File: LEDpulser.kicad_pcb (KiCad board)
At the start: 2 copper layers, 38.2 x 98.2 mm, 72 parts, among them J1 RJHSE5380, J2 EPS.00.250.NTN, J3 EPS.00.250.NTN, J4 Conn_01x04_Female, J5 LED, Q1 AO3401A, Q2 AO3400A, Q3 AO3400A, SW1 BST11T2AVR, U1 SN74AHCT123A, U10 LT3082, U11 SN74HCS72, U2 SN74AHCT123A, U3 SN74AHCT123A, U4 74HC10, U4 SN74AHCT123A, U5 LT1121-5, U6 PM8834, U7 NE555, U8 PM8834, U9 PM8834

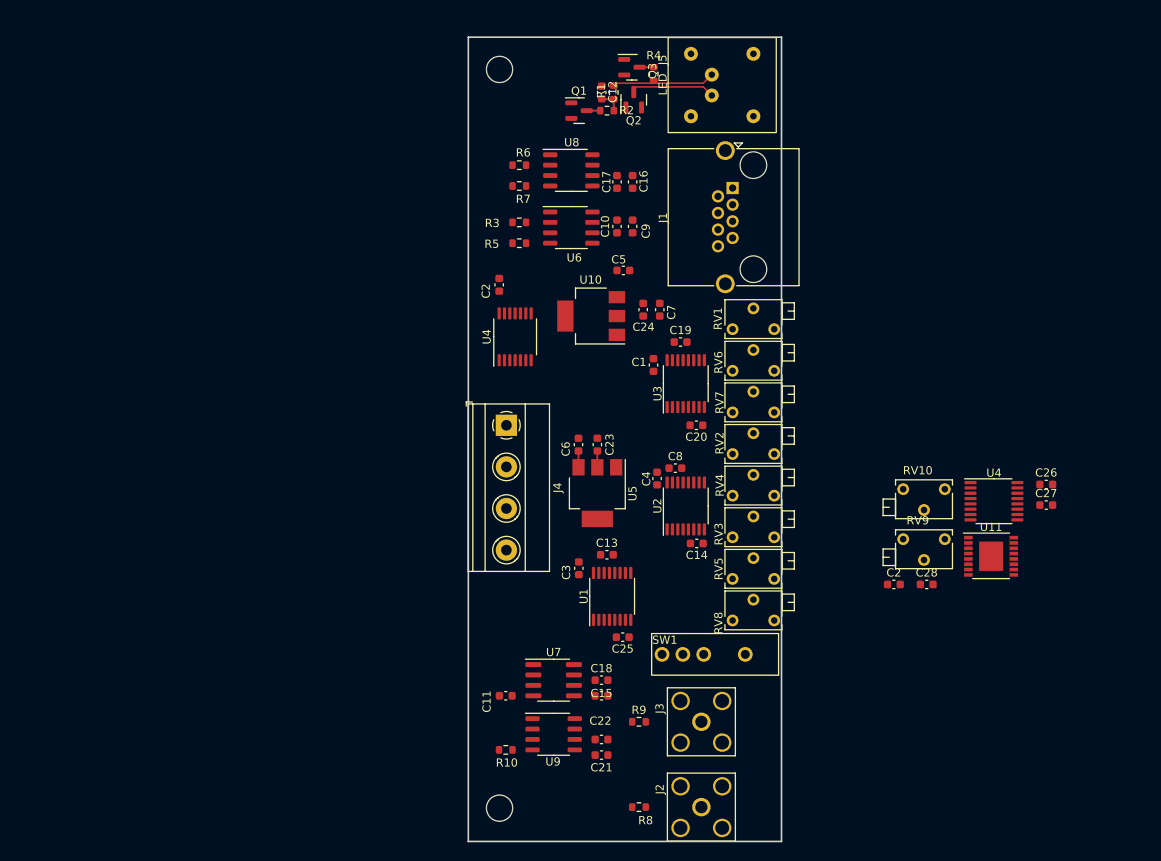
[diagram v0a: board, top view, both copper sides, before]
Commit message: Updated Schematic, started placement.
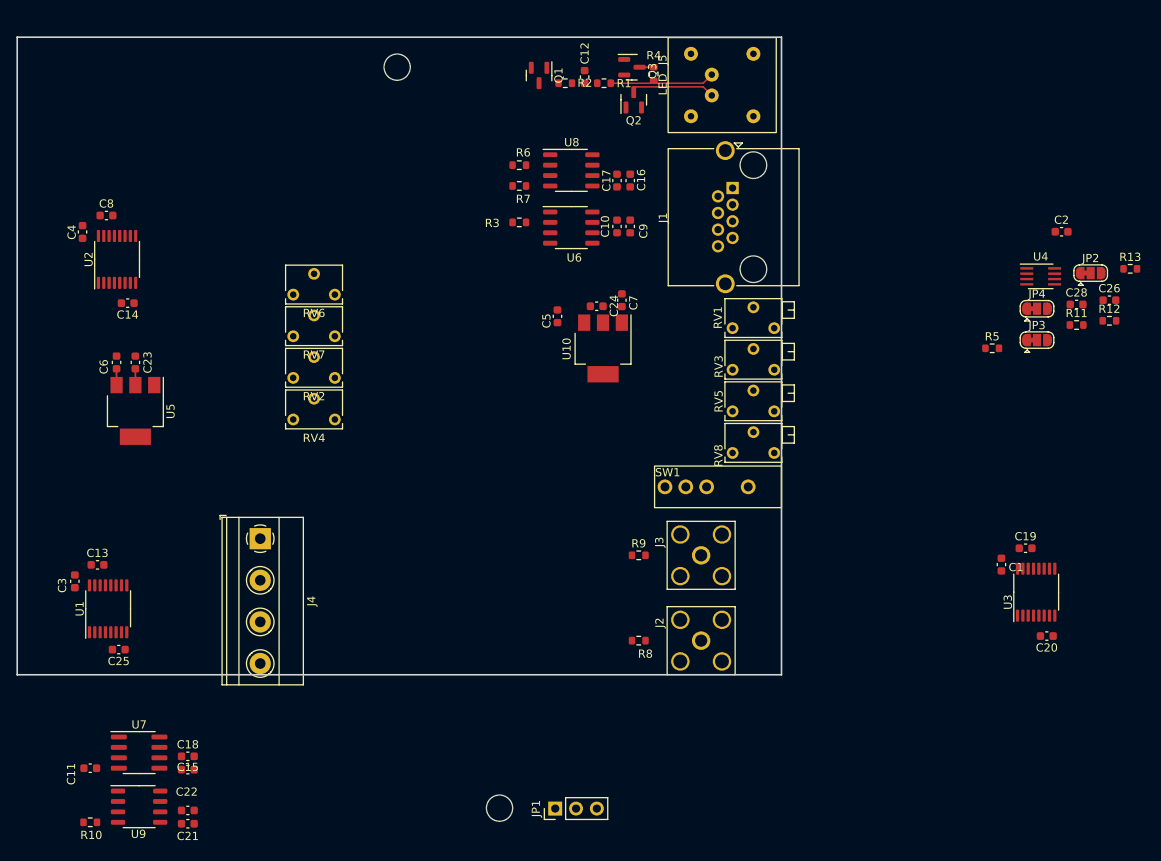
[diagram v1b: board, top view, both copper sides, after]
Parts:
- removed the C2 at (153.4, 92.2)
- removed the C2 at (105.2, 55.6)
- removed C27: 0.1uF, Capacitor_SMD:C_0603_1608Metric
- removed RV10, RV9: 2k, Potentiometer_THT:Potentiometer_Bourns_3266X_Horizontal
- removed U11: SN74HCS72, Package_SO:TSSOP-16-1EP_4.4x5mm_P0.65mm
- removed the U4 at (107.2, 62.0)
- removed the U4 at (165.6, 82.0)
- added C2: 0.1uF, Capacitor_SMD:C_0603_1608Metric, F.Cu at (173.9, 49.1)
- added JP1: Pulse/Clock, Connector_PinHeader_2.54mm:PinHeader_1x03_P2.54mm_Vertical, F.Cu at (112.1, 119.6)
- added JP2: SyncDelay, Jumper:SolderJumper-3_P1.3mm_Bridged12_RoundedPad1.0x1.5mm, F.Cu at (177.4, 54.2)
- added JP3: ShortDelay, Jumper:SolderJumper-3_P1.3mm_Bridged12_RoundedPad1.0x1.5mm, F.Cu at (170.9, 62.4)
- added JP4: LEDdelay, Jumper:SolderJumper-3_P1.3mm_Bridged12_RoundedPad1.0x1.5mm, F.Cu at (170.9, 58.5)
- added R11: 100k, Resistor_SMD:R_0603_1608Metric, F.Cu at (175.7, 60.5)
- added R12: 1k, Resistor_SMD:R_0603_1608Metric, F.Cu at (179.7, 60.0)
- added R13: 100k, Resistor_SMD:R_0603_1608Metric, F.Cu at (182.3, 53.7)
- added U4: SN74LVC2G74, Package_SO:SSOP-8_2.95x2.8mm_P0.65mm, F.Cu at (171.3, 54.6)
- C14, C19, C20, C25, C8: value C -> 1nF
- C26, C28: value C -> 0.1uF
- R2: value 1.2k -> 1k
- R5: value 100k -> 1.2k
- RV2: value 2k -> 1k; footprint Potentiometer_THT:Potentiometer_Bourns_3266X_Horizontal -> Potentiometer_THT:Potentiometer_Bourns_3266W_Vertical
- RV4, RV6, RV7: footprint Potentiometer_THT:Potentiometer_Bourns_3266X_Horizontal -> Potentiometer_THT:Potentiometer_Bourns_3266W_Vertical
- moved C4 76.3 mm to (54.4, 49.2)
- moved C8 76.0 mm to (57.3, 47.2)
- moved U2 75.7 mm to (58.6, 52.5)
- moved C14 75.4 mm to (59.9, 57.9)
- moved C13 62.2 mm to (56.2, 89.8)
- moved C3 61.5 mm to (53.4, 91.8)
- moved C25 61.5 mm to (58.8, 100.2)
- moved U1 61.5 mm to (57.5, 95.2)
- moved R5 59.1 mm to (165.4, 63.4), turned to 0 degrees
- moved C23 57.3 mm to (60.8, 65.1)
- moved C6 57.3 mm to (58.5, 65.1)
- moved U5 57.3 mm to (60.8, 71.0)
- moved RV2 54.4 mm to (80.1, 67.0)
- moved RV4 54.4 mm to (80.1, 72.1)
- moved RV6 54.4 mm to (80.1, 56.8)
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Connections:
- C1 pad 1: +5V -> VCC
- C11 pad 1: +5V -> VCC
- C16 pad 1: +5V -> VCC
- C17 pad 1: +5V -> VCC
- C21 pad 1: +5V -> VCC
- C22 pad 1: +5V -> VCC
- C23 pad 1: +5V -> VCC
- C26 pad 2: Net-(C26-Pad2) -> GND
- C28 pad 1: Net-(U4-Pad15) -> Net-(C28-Pad1)
- C28 pad 2: Net-(U4-Pad14) -> GND
- C3 pad 1: +5V -> VCC
- C4 pad 1: +5V -> VCC
- R5 pad 1: Net-(R5-Pad1) -> VCC
- R5 pad 2: GND -> Net-(C26-Pad1)
- R7 pad 1: Net-(R7-Pad1) -> Net-(U3-Pad5)
- RV2 pad 1: +5V -> VCC
- RV3 pad 1: +5V -> VCC
- RV4 pad 1: +5V -> VCC
- RV6 pad 1: +5V -> VCC
- RV7 pad 1: +5V -> VCC
- RV8 pad 1: +5V -> VCC
- U1 pad 13: unconnected-(U1-Pad13) -> Net-(U1-Pad13)
- U1 pad 16: +5V -> VCC
- U1 pad 3: +5V -> VCC
- U1 pad 4: Net-(U1-Pad4) -> /SYNC_DELAY
- U1 pad 5: Net-(R10-Pad1) -> /SYNC_WIDTH
- U2 pad 10: unconnected-(U2-Pad10) -> Net-(U2-Pad10)
- U2 pad 11: +5V -> Net-(C26-Pad1)
- U2 pad 12: unconnected-(U2-Pad12) -> Net-(U2-Pad12)
- U2 pad 16: +5V -> VCC
- U2 pad 2: unconnected-(U2-Pad2) -> Net-(U1-Pad13)
- U2 pad 3: +5V -> VCC
- U2 pad 4: unconnected-(U2-Pad4) -> Net-(U2-Pad4)
- U2 pad 5: unconnected-(U2-Pad5) -> Net-(R6-Pad1)
- U3 pad 10: unconnected-(U3-Pad10) -> Net-(U3-Pad10)
- U3 pad 11: +5V -> Net-(C28-Pad1)
- U3 pad 12: unconnected-(U3-Pad12) -> Net-(U3-Pad12)
- U3 pad 13: unconnected-(U3-Pad13) -> Net-(U3-Pad13)
- U3 pad 16: +5V -> VCC
- U3 pad 2: unconnected-(U3-Pad2) -> Net-(R6-Pad1)
- U3 pad 3: +5V -> VCC
- U3 pad 5: unconnected-(U3-Pad5) -> Net-(U3-Pad5)
- U5 pad 2: +5V -> VCC
- U6 pad 4: GND -> Net-(R3-Pad1)
- U6 pad 5: unconnected-(U6-Pad5) -> /CAP_CHARGE
- U7 pad 4: +5V -> VCC
- U7 pad 8: +5V -> VCC
- U8 pad 4: Net-(R7-Pad1) -> Net-(U3-Pad5)
- U8 pad 6: +5V -> VCC
- U9 pad 6: +5V -> VCC
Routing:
- net Net-(C12-Pad1): track 2.89 -> 0.00 mm
- net +5V: track 1.99 -> 0.00 mm
- net VCC: track 0.00 -> 1.99 mm
- net Net-(Q1-Pad3): track 1.65 -> 0.00 mm
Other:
- board size 38.2 x 98.2 mm -> 93.3 x 77.8 mm

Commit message: Modified logic to use flip-flop and reduce front panel adjustments. Changed to +24V for LED capacitor charge supply. Selected components. Rough layout.
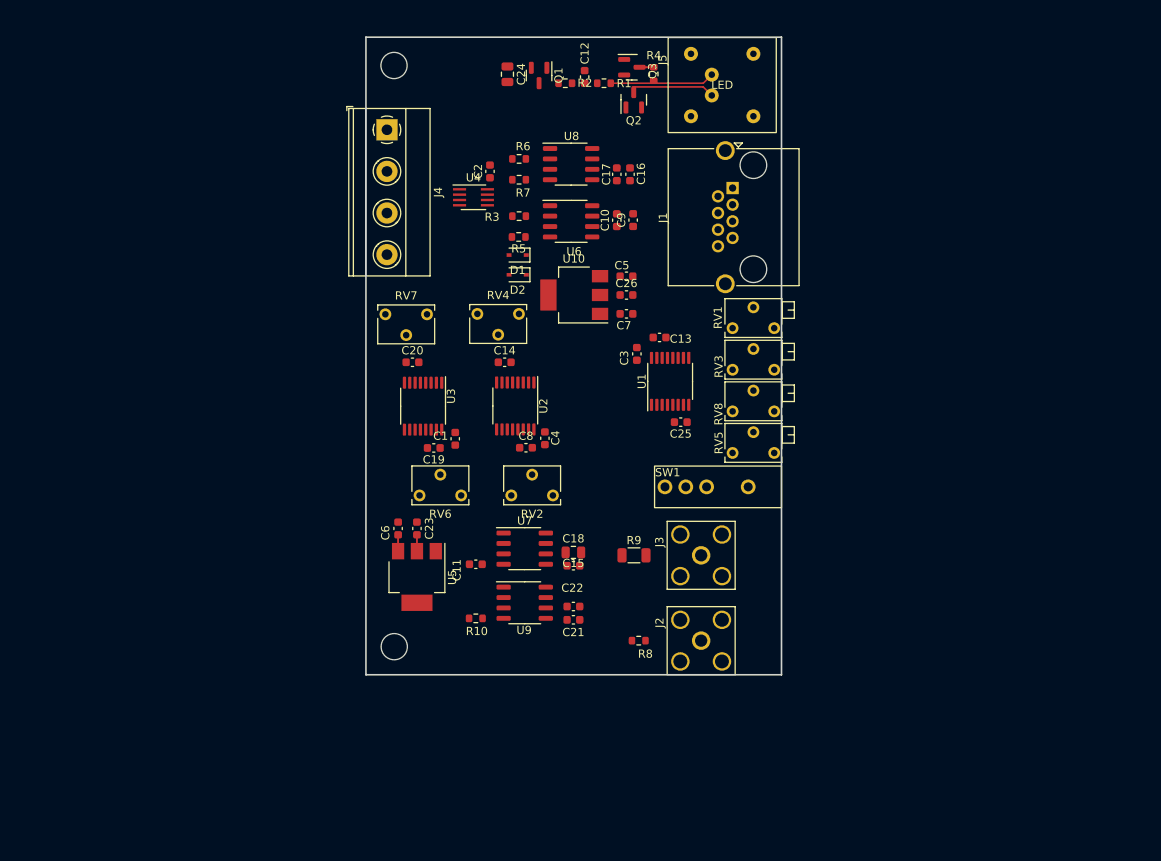
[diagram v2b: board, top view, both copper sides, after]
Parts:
- removed C28: 0.1uF, Capacitor_SMD:C_0603_1608Metric
- removed JP1: Pulse/Clock, Connector_PinHeader_2.54mm:PinHeader_1x03_P2.54mm_Vertical
- removed JP2: SyncDelay, Jumper:SolderJumper-3_P1.3mm_Bridged12_RoundedPad1.0x1.5mm
- removed JP3: ShortDelay, Jumper:SolderJumper-3_P1.3mm_Bridged12_RoundedPad1.0x1.5mm
- removed JP4: LEDdelay, Jumper:SolderJumper-3_P1.3mm_Bridged12_RoundedPad1.0x1.5mm
- removed R11, R13: 100k, Resistor_SMD:R_0603_1608Metric
- removed R12: 1k, Resistor_SMD:R_0603_1608Metric
- added D1: CUS08F30,H3F, Diode_SMD:D_SOD-323, F.Cu at (107.5, 52.0)
- added D2: CUS08F30,H3F, Diode_SMD:D_SOD-323, F.Cu at (107.5, 54.4)
- C18: value 1uF -> 22uF; footprint Capacitor_SMD:C_0603_1608Metric -> Capacitor_SMD:C_0805_2012Metric
- C24: value 4.7uF -> 22uF; footprint Capacitor_SMD:C_0603_1608Metric -> Capacitor_SMD:C_0805_2012Metric
- J1: value RJHSE5380 -> RJHSE-5380
- J4: value Conn_01x04_Female -> EB21A-04-D
- J5: value LED -> EPL.0S.302.HLN
- Q1: value AO3401A -> BVSS84LT1G
- Q2, Q3: value AO3400A -> DMN3028LQ-7
- R5: value 1.2k -> 100k
- R9: footprint Resistor_SMD:R_0603_1608Metric -> Resistor_SMD:R_1206_3216Metric
- RV1: value 1k -> 2k
- RV2, RV3: value 1k -> 500
- RV5: value 1M -> 50k
- U1, U2, U3: value SN74AHCT123A -> 74AHCT123APW,118
- U10: value LT3082 -> LT3082EST#TRPBF
- U5: value LT1121-5 -> LT1121CST-5#TRPBF
- U6: value PM8834 -> IXDI602SIATR
- U7: value NE555 -> NE555S-13; footprint Package_SO:SOIC-8_3.9x4.9mm_P1.27mm -> Package_SO:SO-8_3.9x4.9mm_P1.27mm
- moved C20 84.3 mm to (94.7, 65.1), turned to 0 degrees
- moved U3 78.2 mm to (96.0, 70.4), turned to -90 degrees
- moved C13 74.0 mm to (124.8, 62.1)
- moved C25 74.0 mm to (127.4, 72.4)
- moved C3 74.0 mm to (122.0, 64.1)
- moved U1 74.0 mm to (126.1, 67.4)
- moved C19 73.3 mm to (97.3, 75.5), turned to 180 degrees
- moved C2 70.2 mm to (104.1, 41.8), turned to 90 degrees
- moved U4 69.9 mm to (102.1, 44.9)
- moved C1 68.4 mm to (99.9, 74.4), turned to -90 degrees
- moved C4 61.8 mm to (110.8, 74.4), turned to -90 degrees
- moved R5 59.4 mm to (107.6, 49.8), turned to 180 degrees
- moved C26 59.0 mm to (120.8, 56.9)
- moved C8 58.5 mm to (108.5, 75.5)
- moved C11 53.2 mm to (102.4, 89.7)
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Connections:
- net /EXT renamed Net-(J2-Pad1)
- net /INT renamed /INTERNAL
- net Net-(SW1-Pad2) renamed /INPUT
- net Net-(SW1-Pad3) renamed /EXTERNAL
- net Net-(U3-Pad12) renamed /CAP_CHARGE_ON
- C10 pad 1: +12V -> Net-(C10-Pad1)
- C24 pad 1: /CAP_VOLTAGE -> /CAP_VOLTAGE_OUT
- C26 pad 1: Net-(C26-Pad1) -> /CAP_VOLTAGE_OUT
- C5 pad 1: +12V -> +24V
- C9 pad 1: +12V -> Net-(C10-Pad1)
- J1 pad 2: /LED_SHORT -> /LED_SHORT_OUT
- J1 pad 4: /LED_ON -> /LED_ON_OUT
- J1 pad 6: /CAP_CHARGE -> /CAP_CHARGING_OUT
- J1 pad 8: /CAP_VOLTAGE -> /CAP_VOLTAGE_OUT
- J3 pad 1: /SYNC -> Net-(J3-Pad1)
- J4 pad 1: +12V -> +24V
- Q1 pad 1: /CAP_CHARGE -> /CAP_CHARGING_OUT
- Q1 pad 2: /CAP_VOLTAGE -> /CAP_VOLTAGE_OUT
- Q2 pad 1: /LED_ON -> /LED_ON_OUT
- Q3 pad 1: /LED_SHORT -> /LED_SHORT_OUT
- R10 pad 1: Net-(R10-Pad1) -> /SYNC
- R3 pad 1: Net-(R3-Pad1) -> Net-(U4-Pad5)
- R5 pad 1: VCC -> Net-(U6-Pad4)
- R5 pad 2: Net-(C26-Pad1) -> GND
- R6 pad 1: Net-(R6-Pad1) -> /LED_ON
- R7 pad 1: Net-(U3-Pad5) -> /LED_SHORT
- R9 pad 2: /SYNC -> Net-(J3-Pad1)
- RV2 pad 2: Net-(C8-Pad1) -> Net-(C8-Pad2)
- RV2 pad 3: Net-(C8-Pad1) -> Net-(C8-Pad2)
- U1 pad 10: Net-(U1-Pad10) -> /SYNC_DELAY
- U1 pad 5: /SYNC_WIDTH -> /SYNC
- U10 pad 2: /CAP_VOLTAGE -> /CAP_VOLTAGE_OUT
- U10 pad 3: +12V -> +24V
- U2 pad 10: Net-(U2-Pad10) -> Net-(U3-Pad2)
- U2 pad 11: Net-(C26-Pad1) -> VCC
- U2 pad 12: Net-(U2-Pad12) -> unconnected-(U2-Pad12)
- U2 pad 14: Net-(C8-Pad2) -> Net-(C8-Pad1)
- U2 pad 15: Net-(C8-Pad1) -> Net-(C8-Pad2)
- U2 pad 4: Net-(U2-Pad4) -> Net-(U3-Pad2)
- U2 pad 5: Net-(R6-Pad1) -> /LED_ON
- U3 pad 10: Net-(U3-Pad10) -> /LED_SHORT_DELAY
- U3 pad 11: Net-(C28-Pad1) -> VCC
- U3 pad 13: Net-(U3-Pad13) -> /LED_SHORT_DELAY
- U3 pad 2: Net-(R6-Pad1) -> Net-(U3-Pad2)
- U3 pad 5: Net-(U3-Pad5) -> /LED_SHORT
- U4 pad 5: Net-(R3-Pad1) -> Net-(U4-Pad5)
- U6 pad 2: Net-(R3-Pad1) -> Net-(U4-Pad5)
- U6 pad 4: Net-(R3-Pad1) -> Net-(U6-Pad4)
- U6 pad 5: /CAP_CHARGE -> unconnected-(U6-Pad5)
- U6 pad 6: +12V -> Net-(C10-Pad1)
- U6 pad 7: /CAP_CHARGE -> /CAP_CHARGING_OUT
- U8 pad 2: Net-(R6-Pad1) -> /LED_ON
- U8 pad 4: Net-(U3-Pad5) -> /LED_SHORT
- U8 pad 5: /LED_SHORT -> /LED_SHORT_OUT
- U8 pad 7: /LED_ON -> /LED_ON_OUT
- U9 pad 4: Net-(R10-Pad1) -> /SYNC
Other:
- board size 93.3 x 77.8 mm -> 50.7 x 77.8 mm

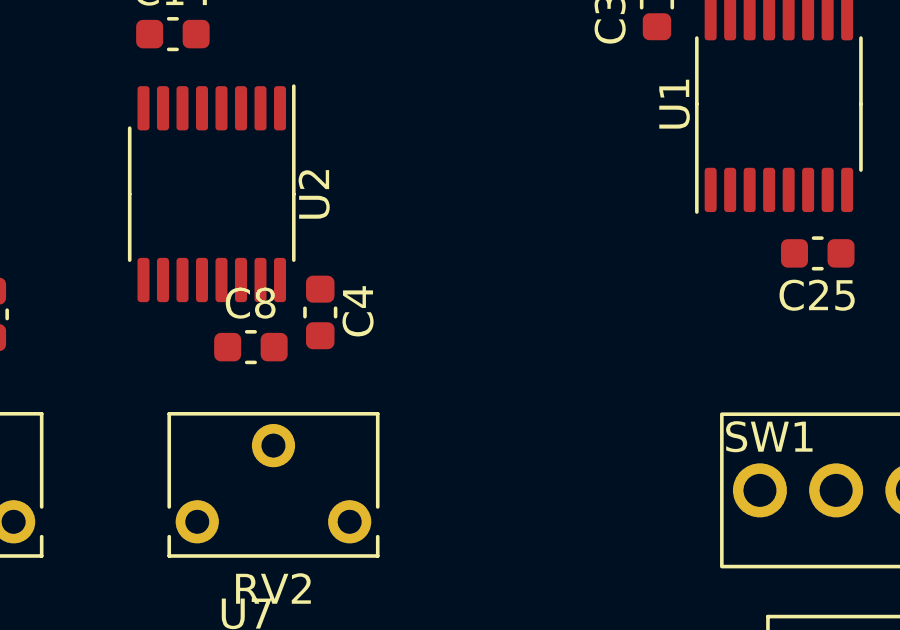
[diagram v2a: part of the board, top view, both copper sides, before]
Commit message: Fixed logic on LED short delay and added startup inhibit to set initial states.
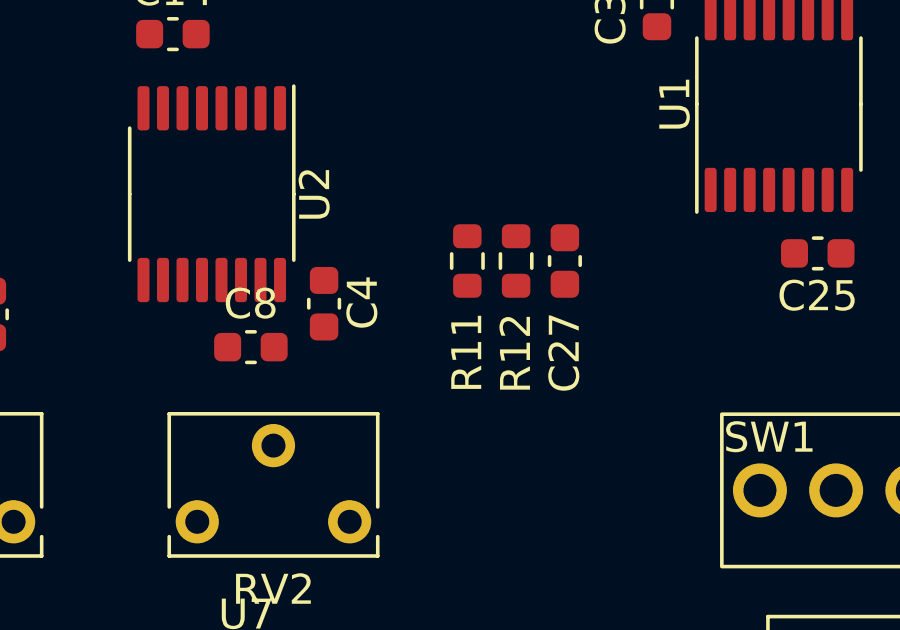
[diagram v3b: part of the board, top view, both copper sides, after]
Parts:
- added C27: 0.1uF, Capacitor_SMD:C_0603_1608Metric, F.Cu at (119.0, 72.6)
- added R11: 10k, Resistor_SMD:R_0603_1608Metric, F.Cu at (115.7, 72.6)
- added R12: 100k, Resistor_SMD:R_0603_1608Metric, F.Cu at (117.3, 72.6)
- moved C4 0.32 mm to (110.9, 74.1)
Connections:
- U2 pad 11: VCC -> SU_INHIBIT
- U3 pad 11: VCC -> SU_INHIBIT
- U3 pad 13: /LED_SHORT_DELAY -> unconnected-(U3-Pad13)
- U3 pad 4: unconnected-(U3-Pad4) -> /LED_SHORT_DELAY
- U4 pad 6: VCC -> SU_INHIBIT

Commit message: Routed
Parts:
- RV5: value 50k -> 100k
- moved C24 5.66 mm to (111.5, 27.8), turned to 0 degrees
- moved D2 3.40 mm to (104.1, 54.8)
- moved D1 3.38 mm to (104.1, 51.9)
- moved R7 2.85 mm to (108.9, 40.2)
- moved R6 2.81 mm to (108.9, 42.8)
- moved J4 2.08 mm to (93.6, 36.7)
- moved C16 1.66 mm to (122.9, 42.3)
- moved C17 1.25 mm to (120.8, 42.3)
- moved U4 1.24 mm to (103.3, 44.9)
- moved C9 1.24 mm to (122.8, 47.7)
- moved R3 1.24 mm to (108.9, 47.2)
- moved R5 1.24 mm to (108.9, 49.8)
- moved C10 1.24 mm to (120.8, 47.7)
- moved U6 1.24 mm to (115.3, 47.9)
- moved U8 1.24 mm to (115.3, 40.9)
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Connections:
- U8 pad 2: /LED_ON -> /LED_SHORT
- U8 pad 4: /LED_SHORT -> /LED_ON
- U8 pad 5: /LED_SHORT_OUT -> /LED_ON_OUT
- U8 pad 7: /LED_ON_OUT -> /LED_SHORT_OUT
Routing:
- net VCC: track 1.99 -> 253.2 mm, vias 0 -> 3
- net /SYNC: track 0.00 -> 77.2 mm
- net /CAP_VOLTAGE_OUT: track 0.00 -> 76.3 mm, vias 0 -> 1
- net SU_INHIBIT: track 0.00 -> 55.9 mm, vias 0 -> 3
- net /LED_SHORT_OUT: track 0.00 -> 46.1 mm
- net Net-(C18-Pad1): track 0.00 -> 41.7 mm
- net /LED_ON: track 0.00 -> 41.4 mm
- net /LED_SHORT: track 0.00 -> 41.4 mm
- net /SYNC_DELAY: track 0.00 -> 38.8 mm, vias 0 -> 2
- net /INTERNAL: track 0.00 -> 36.1 mm
- net +6V: track 1.99 -> 37.2 mm
- net +24V: track 0.00 -> 33.7 mm, vias 0 -> 1
- net /CAP_CHARGING_OUT: track 0.00 -> 33.4 mm
- net /CAP_CHARGE_ON: track 0.00 -> 32.7 mm, vias 0 -> 2
- net /LED_ON_OUT: track 0.00 -> 26.9 mm
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- added copper zone on B.Cu, net GND
- added copper zone on F.Cu, net GND
